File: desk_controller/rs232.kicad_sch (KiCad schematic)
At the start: 14 parts

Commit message: Sch work
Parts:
- removed U?: Si8640BA-B-IU, Package_SO:QSOP-16_3.9x4.9mm_P0.635mm, symbol Isolator:Si8640BA-B-IU
- added C? (x2): 1u, Capacitor_SMD:C_0603_1608Metric, symbol Device:C
- added U?: AP2112K-3.3, Package_TO_SOT_SMD:SOT-23-5, symbol Regulator_Linear:AP2112K-3.3
- added U?: ISO7721DR, SOIC127P599X175-8N, symbol ISO7721DR:ISO7721DR
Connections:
- net 232_VCC: now also C?.1, U?.5 (VOUT)
- net 232_VUR: now also C?.1, U?.1 (VIN), U?.3 (EN)
- net GND1: now also C?.2, C?.2, U?.2 (GND)
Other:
- note added: "- LDO is 600mA max - Pd = (Vi-V0) * I = (12-3.3)*0.4 ="
- note added: "- data speed is bps"
- note added: "TODO check if LDO can withstand current draw or transceiver and isolator combined"

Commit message: Added components
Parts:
- removed D? (x2): D_Schottky, symbol Device:D_Schottky
- removed R? (x4): R, symbol Device:R
- removed U?: ISO7721DR, SOIC127P599X175-8N, symbol ISO7721DR:ISO7721DR
- removed U?: SN74LVC2G04DCKR, SN74LVC2G04DCKR:SOT65P210X110-6N, symbol SN74LVC2G04DCKR:SN74LVC2G04DCKR
- added C?: 100n, symbol Device:C
- added R? (x2): R, symbol Device:R
- added U? (x2): PC817, Package_DIP:DIP-4_W7.62mm, symbol Isolator:PC817
- added U?: ISO7341FC, Package_SO:SOIC-16W_7.5x10.3mm_P1.27mm, symbol Isolator:ISO7341FC
- C?: value C -> 100n
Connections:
- net 232_DTR: now also U?.4 (INB)
- net 232_RTS: now also U?.5 (INC)
- net 232_RX: now also U?.6 (OUTD)
- net 232_TX: now also U?.3 (INA)
- net 232_VCC: now also C?.1, U?.1 (VCC1), U?.7 (EN1)
- net GND: now also U?.2, U?.2
- net GND1: now also C?.1, C?.2, U?.15 (GND2), U?.2 (GND1), U?.8 (GND1), U?.9 (GND2)
- net POWER+: now also U?.4
- net RESET+: now also U?.4
- net +3.3V: now reaches C?.2
- net +3.3V: now also U?.10 (EN2), U?.16 (VCC2)
- new net: R?.2, U?.1 (x2)
- new net GND2: U?.3, U?.3
- new net POWER_SIG: R?.1
- new net RESET_SIG: R?.1
- new net TTL_DTR: U?.13 (OUTB)
- new net TTL_RTS: U?.12 (OUTC)
- new net TTL_RX: U?.11 (IND)
- new net TTL_TX: U?.14 (OUTA)
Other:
- note added: "TRS3243ECRHBR"
- note added: "optos are APC-817D1-SL"
- note removed: "check orientation of this component"
- moved on the sheet: C?

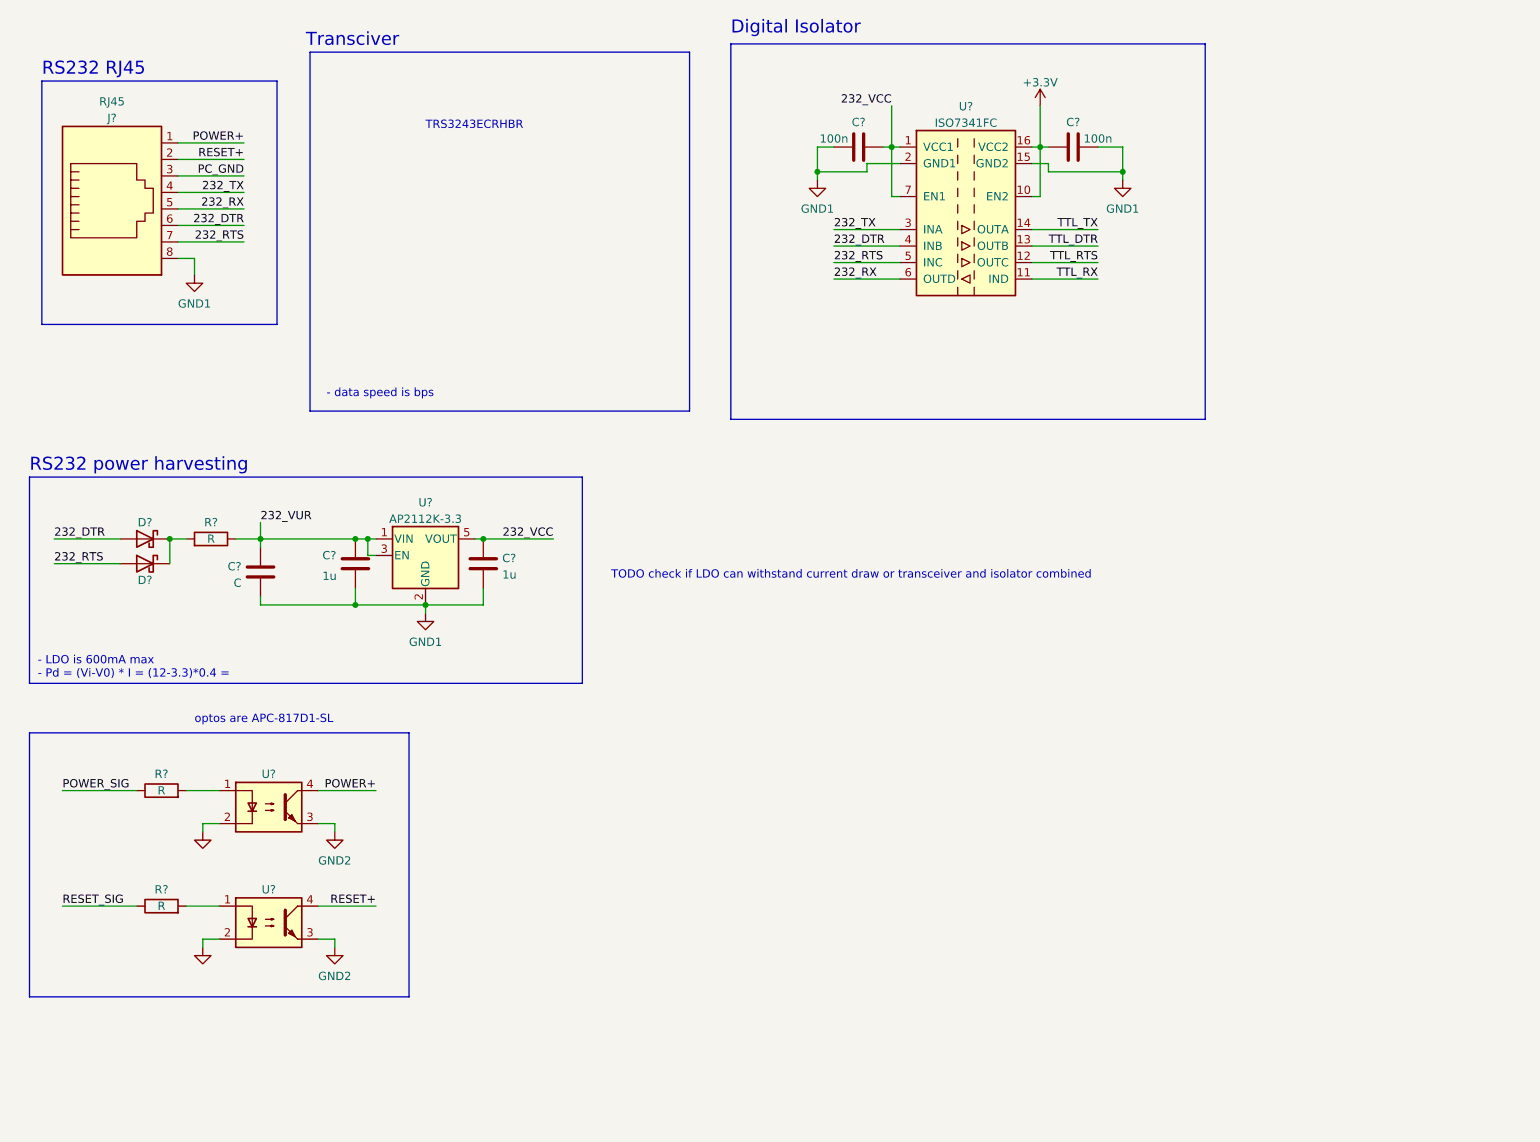
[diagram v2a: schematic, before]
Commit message: Buck converter sch, rs232 transceiver
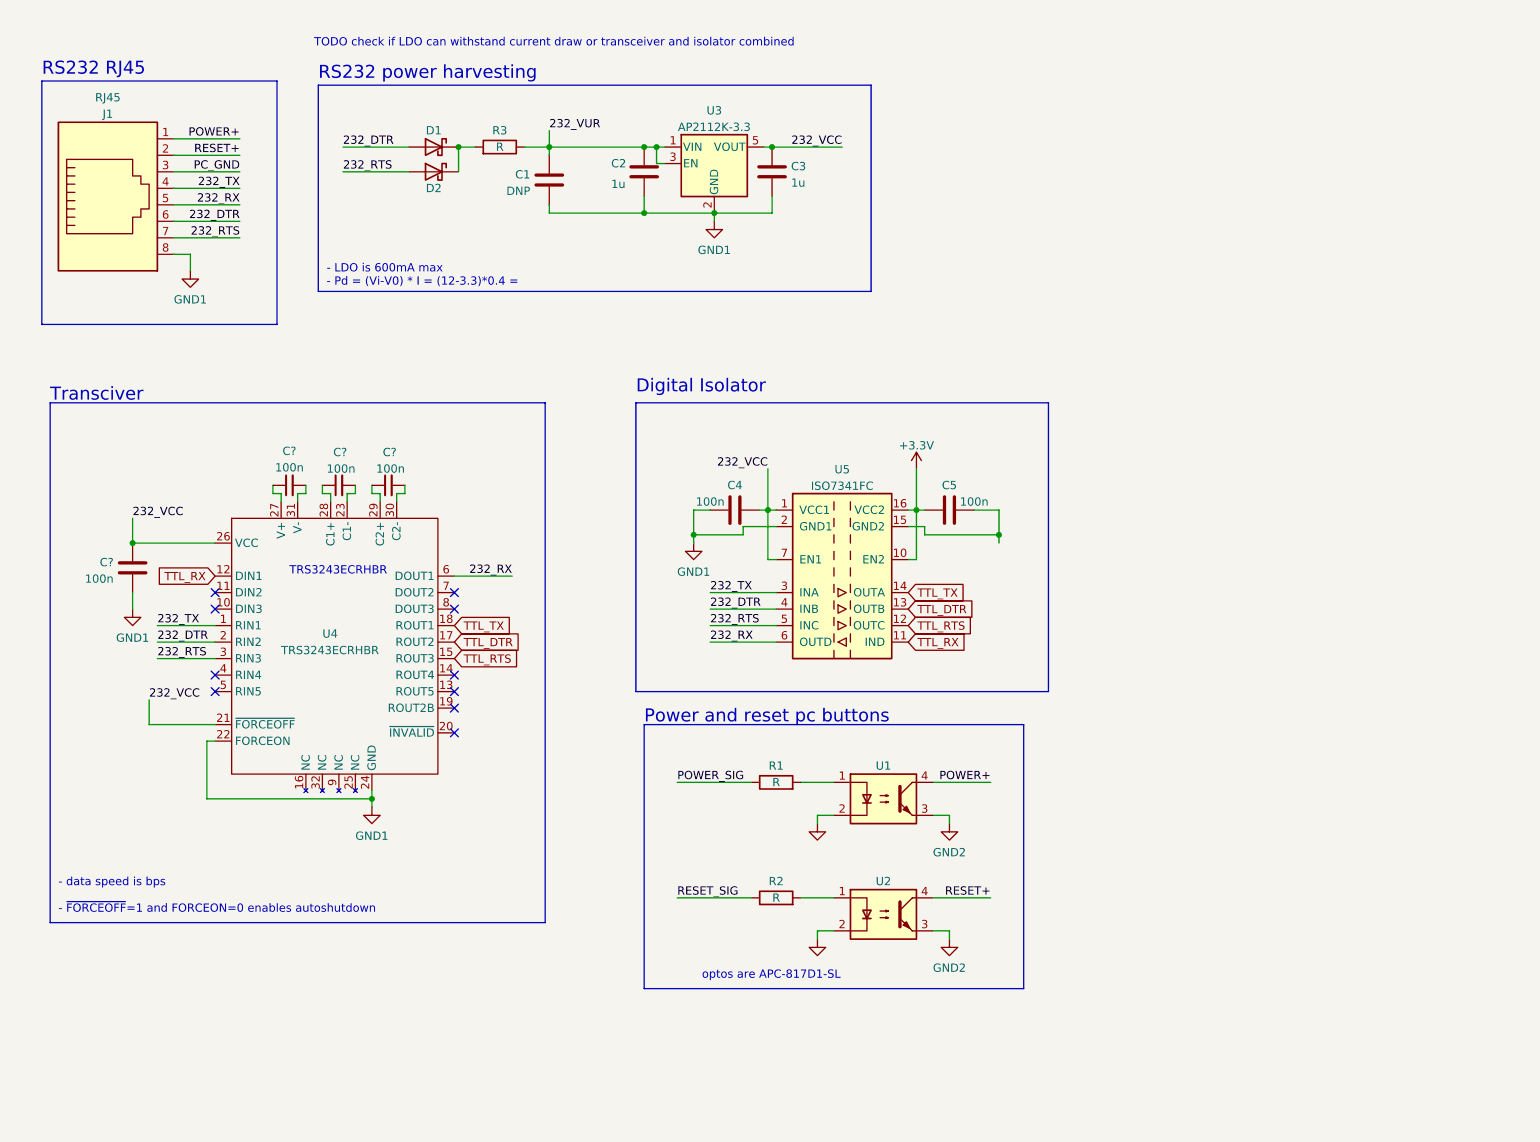
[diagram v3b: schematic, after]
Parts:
- added C? (x3): 100n, symbol Device:C_Small
- added C?: 100n, symbol Device:C
- added U4: TRS3243ECRHBR, Package_DFN_QFN:VQFN-32-1EP_5x5mm_P0.5mm_EP3.5x3.5mm, symbol TRS3243ECRHBR:TRS3243ECRHBR
- C1: renamed from C?; value C -> DNP
- gave numbers to parts that had none: 14
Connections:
- net 232_DTR: now also U4.2 (RIN2)
- net 232_RTS: now also U4.3 (RIN3)
- net 232_RX: now also U4.6 (DOUT1)
- net 232_TX: now also U4.1 (RIN1)
- net 232_VCC: now also C?.1, U4.21 (~{FORCEOFF}), U4.26 (VCC)
- net GND1: now also C?.2, U4.22 (FORCEON), U4.24 (GND); no longer C5.1, U5.15 (GND2), U5.9 (GND2)
- net TTL_DTR: now also U4.17 (ROUT2)
- net TTL_RTS: now also U4.15 (ROUT3)
- net TTL_RX: now also U4.12 (DIN1)
- net TTL_TX: now also U4.18 (ROUT1)
- new net: C5.1, U5.15 (GND2), U5.9 (GND2)
- new net: C?.1, U4.29 (C2+)
- new net: C?.2, U4.30 (C2-)
- new net: C?.1, U4.27 (V+)
- new net: C?.2, U4.31 (V-)
- new net: C?.2, U4.23 (C1-)
- new net: C?.1, U4.28 (C1+)
- no-connect marks 0 -> 10
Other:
- note added: "- data speed is bps - ~{FORCEOFF}=1 and FORCEON=0 enables autoshutdown"
- note added: "Power and reset pc buttons"
- note removed: "- data speed is bps"
- moved on the sheet: C1, C2, C3, C4, C5, D1, D2, J1, R1, R2, R3, U1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

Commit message: Sch fixes, initial board layout
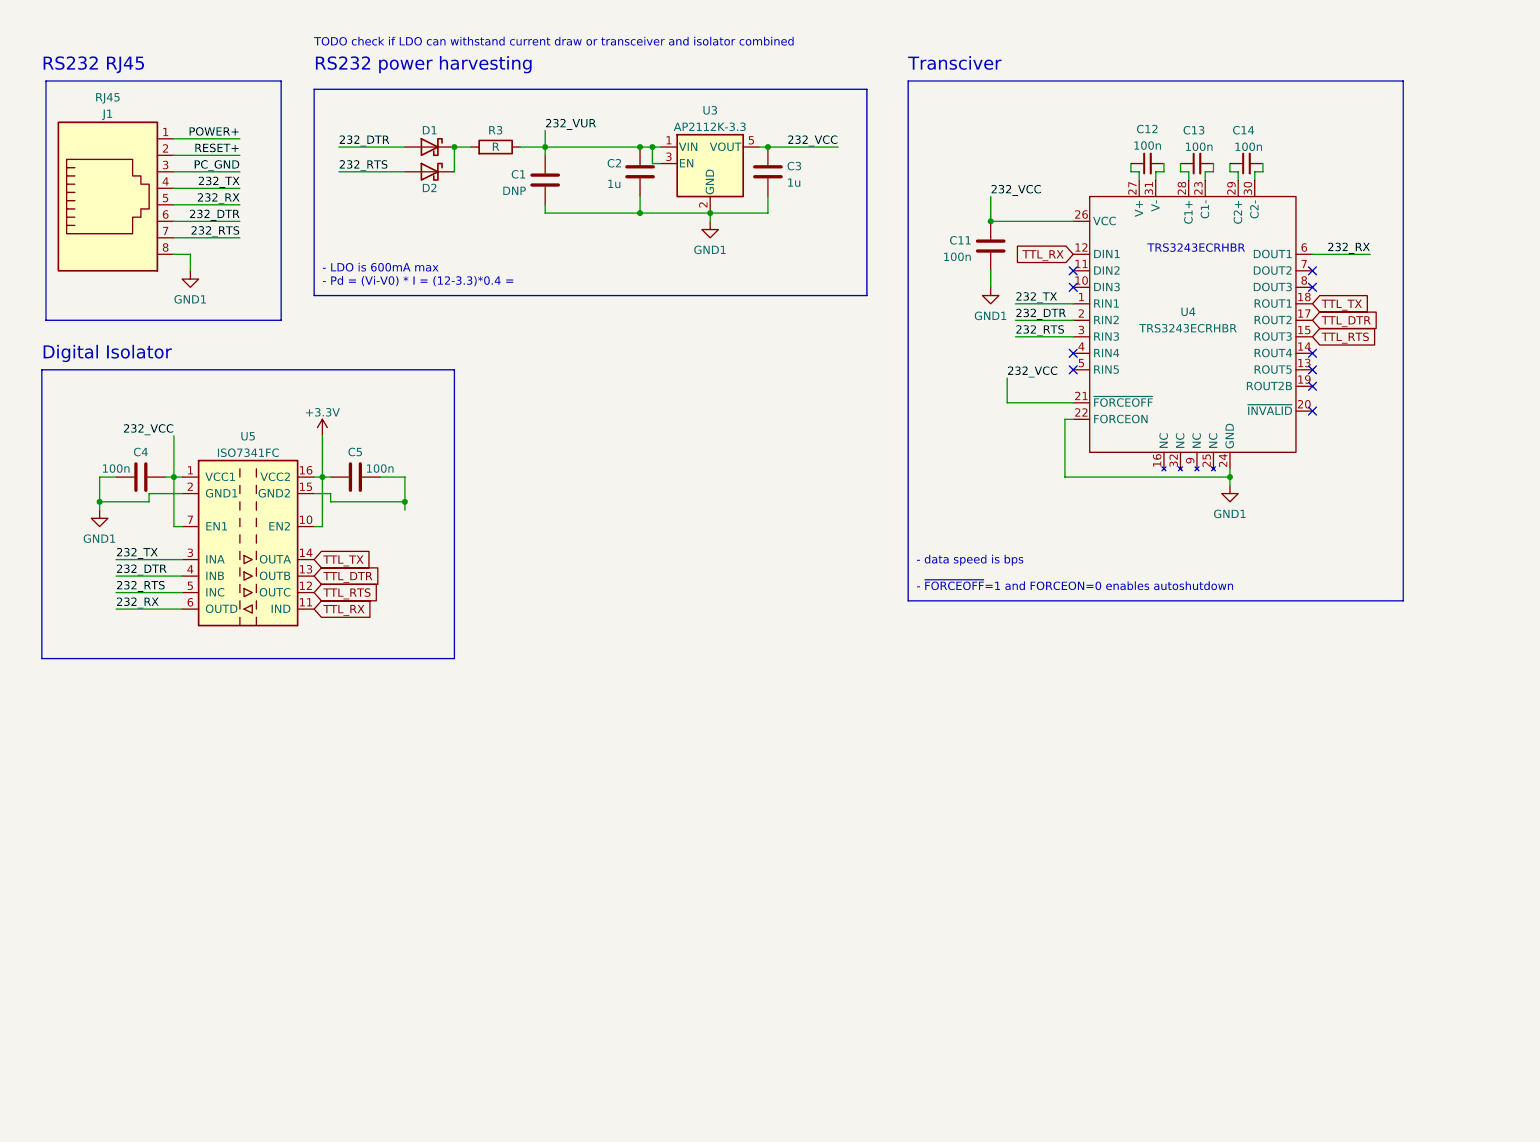
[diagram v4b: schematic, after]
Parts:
- removed R1, R2: R, symbol Device:R
- removed U1, U2: PC817, Package_DIP:DIP-4_W7.62mm, symbol Isolator:PC817
- C1, C4, C5: footprint (none) -> Capacitor_SMD:C_0603_1608Metric
- C11, C12, C13, C14: renamed from C?; footprint (none) -> Capacitor_SMD:C_0603_1608Metric
- R3: footprint (none) -> Resistor_SMD:R_0603_1608Metric
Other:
- note removed: "Power and reset pc buttons"
- note removed: "optos are APC-817D1-SL"
- moved on the sheet: C1, C11, C12, C13, C14, C2, C3, C4, C5, D1, D2, R3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

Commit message: Much progress in sch and brd
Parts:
- D1, D2: footprint (none) -> Diode_SMD:D_0805_2012Metric
- J1: footprint (none) -> Connector_RJ:RJ45_Ninigi_GE
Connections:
- net 232_DTR: no longer U5.4 (INB)
- net 232_RTS: no longer U5.5 (INC)
- net 232_RX: no longer U5.6 (OUTD)
- net 232_TX: no longer U5.3 (INA)
- net TTL_DTR: now also U5.4 (INB); no longer U5.13 (OUTB)
- net TTL_RTS: now also U5.5 (INC); no longer U5.12 (OUTC)
- net TTL_RX: now also U5.6 (OUTD); no longer U5.11 (IND)
- net TTL_TX: now also U5.3 (INA); no longer U5.14 (OUTA)
- net GND: now reaches C5.1, U5.15 (GND2), U5.9 (GND2)
- net POWER+ renamed POWER
- net RESET+ renamed RESET
- new net TTL_DTR_ISO: U5.13 (OUTB)
- new net TTL_RTS_ISO: U5.12 (OUTC)
- new net TTL_RX_ISO: U5.11 (IND)
- new net TTL_TX_ISO: U5.14 (OUTA)
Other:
- note added: "- GND1 is RS232 GND - PC_GND is GND coming from PC motherboard - GND is GND from STM32 circuit"
- note removed: "TRS3243ECRHBR"
- moved on the sheet: C1, C11, C12, C13, C14, C2, C3, C4, C5, D1, D2, J1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
